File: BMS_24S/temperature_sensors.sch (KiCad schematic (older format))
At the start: 27 parts, among them J1501 TEMP_IDC_26_CONN

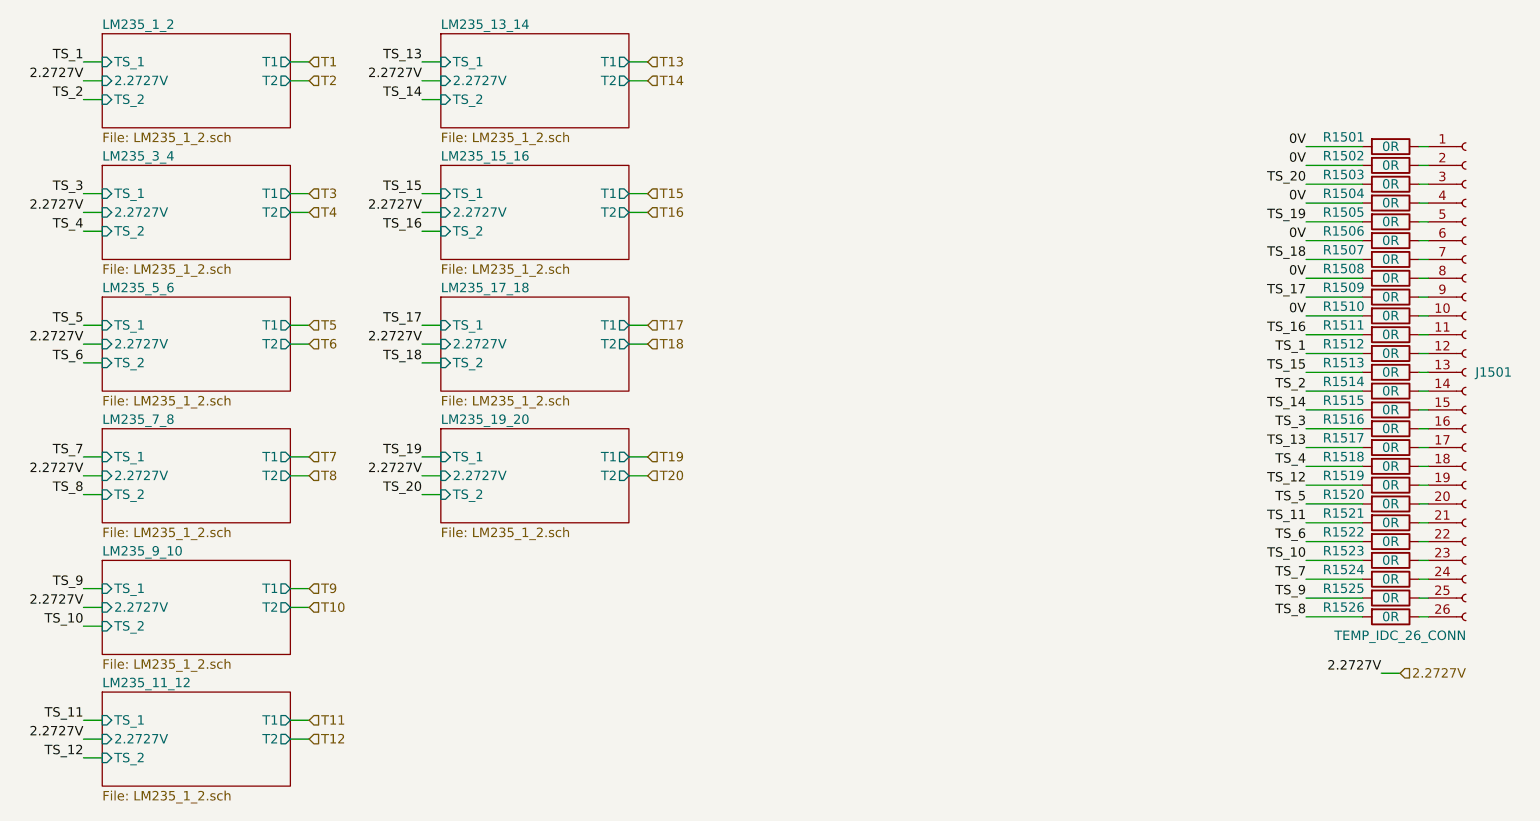
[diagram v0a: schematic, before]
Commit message: update balancing circuit
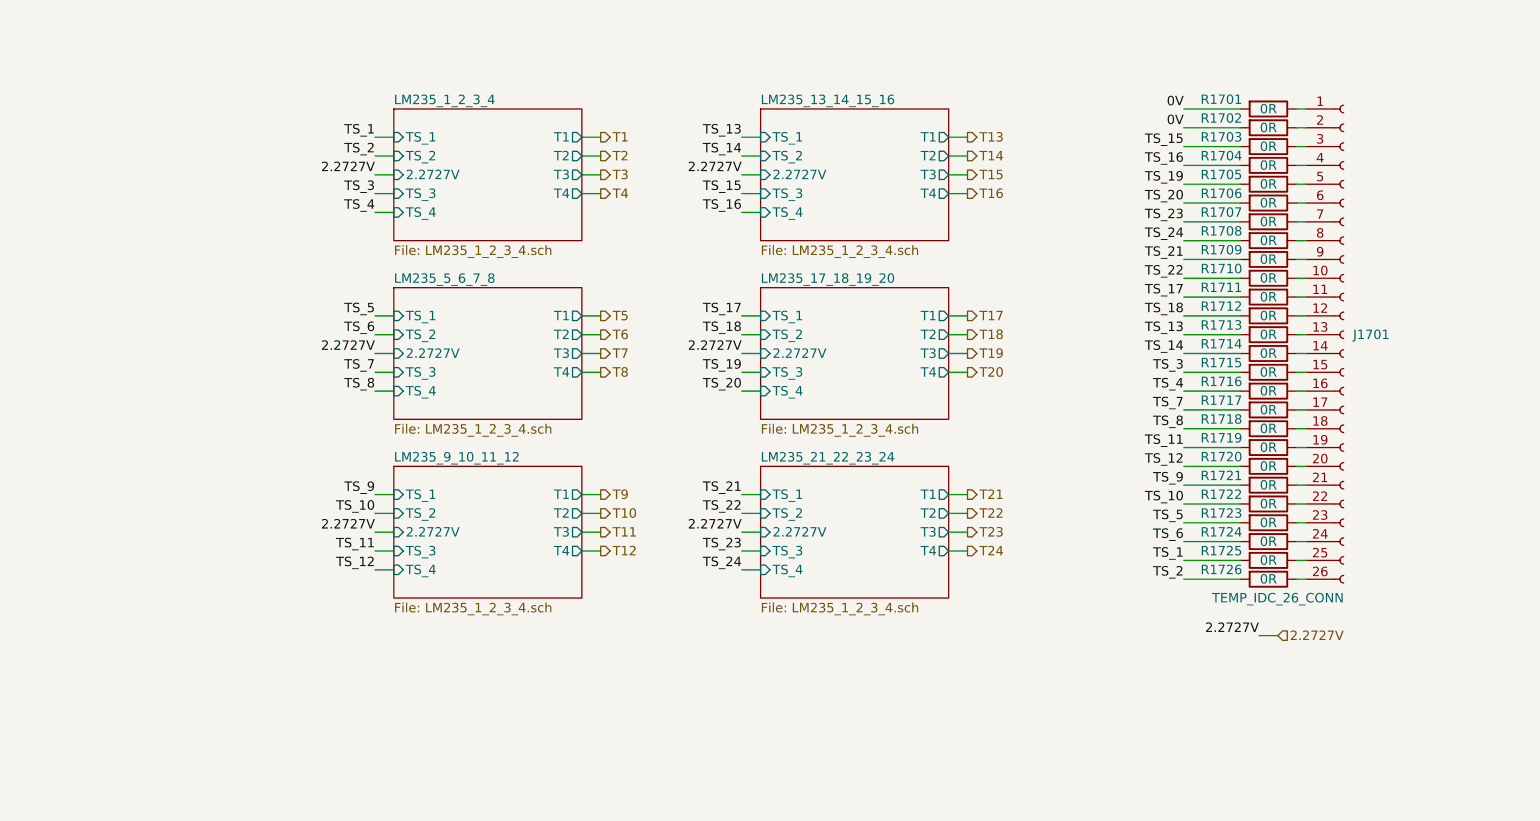
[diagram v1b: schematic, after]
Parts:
- renumbered J1501 to J1701, R1501 to R1701, R1502 to R1702, R1503 to R1703, R1504 to R1704, R1505 to R1705, R1506 to R1706, R1507 to R1707, R1508 to R1708, R1509 to R1709, R1510 to R1710, R1511 to R1711, R1512 to R1712, R1513 to R1713, R1514 to R1714, R1515 to R1715, R1516 to R1716, R1517 to R1717, R1518 to R1718, R1519 to R1719, R1520 to R1720, R1521 to R1721, R1522 to R1722, R1523 to R1723, R1524 to R1724, R1525 to R1725, R1526 to R1726
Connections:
- net 0V: no longer R1704.2, R1706.2, R1708.2, R1710.2
- net TS_1: now also R1725.2; no longer R1712.2
- net TS_10: now also R1722.2; no longer R1723.2
- net TS_11: now also R1719.2; no longer R1721.2
- net TS_12: now also R1720.2; no longer R1719.2
- net TS_13: now also R1713.2; no longer R1717.2
- net TS_14: now also R1714.2; no longer R1715.2
- net TS_15: now also R1703.2; no longer R1713.2
- net TS_16: now also R1704.2; no longer R1711.2
- net TS_17: now also R1711.2; no longer R1709.2
- net TS_18: now also R1712.2; no longer R1707.2
- net TS_2: now also R1726.2; no longer R1714.2
- net TS_20: now also R1706.2; no longer R1703.2
- net TS_3: now also R1715.2; no longer R1716.2
- net TS_4: now also R1716.2; no longer R1718.2
- net TS_5: now also R1723.2; no longer R1720.2
- net TS_6: now also R1724.2; no longer R1722.2
- net TS_7: now also R1717.2; no longer R1724.2
- net TS_8: now also R1718.2; no longer R1726.2
- net TS_9: now also R1721.2; no longer R1725.2
- new net TS_21: R1709.2
- new net TS_22: R1710.2
- new net TS_23: R1707.2
- new net TS_24: R1708.2
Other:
- moved on the sheet: J1701, R1701, R1702, R1703, R1704, R1705, R1706, R1707, R1708, R1709, R1710, R1711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

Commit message: get BSPD
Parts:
- R1701, R1702, R1703, R1704, R1705, R1706, R1707, R1708, R1709, R1710, R1711, R1712, R1713, R1714, R1715, R1716, R1717, R1718, R1719, R1720, R1721, R1722, R1723, R1724, R1725, R1726: LCSC (none) -> C17477
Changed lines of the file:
@@
 F 2 "Resistor_SMD:R_0805_2012Metric" V 7080 1100 50  0001 C CNN
 F 3 "~" H 7150 1100 50  0001 C CNN
+F 4 "C17477" H 7150 1100 50  0001 C CNN "LCSC"
 	1    7150 1100
 	0    1    1    0
@@
 F 2 "Resistor_SMD:R_0805_2012Metric" V 7080 1200 50  0001 C CNN
 F 3 "~" H 7150 1200 50  0001 C CNN
+F 4 "C17477" H 7150 1200 50  0001 C CNN "LCSC"
 	1    7150 1200
 	0    1    1    0
@@
 F 2 "Resistor_SMD:R_0805_2012Metric" V 7080 1300 50  0001 C CNN
 F 3 "~" H 7150 1300 50  0001 C CNN
+F 4 "C17477" H 7150 1300 50  0001 C CNN "LCSC"
 	1    7150 1300
 	0    1    1    0
@@
 F 2 "Resistor_SMD:R_0805_2012Metric" V 7080 1400 50  0001 C CNN
 F 3 "~" H 7150 1400 50  0001 C CNN
+F 4 "C17477" H 7150 1400 50  0001 C CNN "LCSC"
 	1    7150 1400
 	0    1    1    0
@@
 F 2 "Resistor_SMD:R_0805_2012Metric" V 7080 1500 50  0001 C CNN
 F 3 "~" H 7150 1500 50  0001 C CNN
+F 4 "C17477" H 7150 1500 50  0001 C CNN "LCSC"
 	1    7150 1500
 	0    1    1    0
@@
 F 2 "Resistor_SMD:R_0805_2012Metric" V 7080 1600 50  0001 C CNN
 F 3 "~" H 7150 1600 50  0001 C CNN
+F 4 "C17477" H 7150 1600 50  0001 C CNN "LCSC"
 	1    7150 1600
 	0    1    1    0
@@
 F 2 "Resistor_SMD:R_0805_2012Metric" V 7080 1700 50  0001 C CNN
 F 3 "~" H 7150 1700 50  0001 C CNN
+F 4 "C17477" H 7150 1700 50  0001 C CNN "LCSC"
 	1    7150 1700
 	0    1    1    0
@@
 F 2 "Resistor_SMD:R_0805_2012Metric" V 7080 1800 50  0001 C CNN
 F 3 "~" H 7150 1800 50  0001 C CNN
+F 4 "C17477" H 7150 1800 50  0001 C CNN "LCSC"
 	1    7150 1800
 	0    1    1    0
@@
 F 2 "Resistor_SMD:R_0805_2012Metric" V 7080 1900 50  0001 C CNN
 F 3 "~" H 7150 1900 50  0001 C CNN
+F 4 "C17477" H 7150 1900 50  0001 C CNN "LCSC"
 	1    7150 1900
 	0    1    1    0
@@
 F 2 "Resistor_SMD:R_0805_2012Metric" V 7080 2000 50  0001 C CNN
 F 3 "~" H 7150 2000 50  0001 C CNN
+F 4 "C17477" H 7150 2000 50  0001 C CNN "LCSC"
 	1    7150 2000
 	0    1    1    0
@@
 F 2 "Resistor_SMD:R_0805_2012Metric" V 7080 2100 50  0001 C CNN
 F 3 "~" H 7150 2100 50  0001 C CNN
+F 4 "C17477" H 7150 2100 50  0001 C CNN "LCSC"
 	1    7150 2100
 	0    1    1    0
@@
 F 2 "Resistor_SMD:R_0805_2012Metric" V 7080 2400 50  0001 C CNN
 F 3 "~" H 7150 2400 50  0001 C CNN
+F 4 "C17477" H 7150 2400 50  0001 C CNN "LCSC"
 	1    7150 2400
 	0    1    1    0
@@
 F 2 "Resistor_SMD:R_0805_2012Metric" V 7080 2200 50  0001 C CNN
 F 3 "~" H 7150 2200 50  0001 C CNN
+F 4 "C17477" H 7150 2200 50  0001 C CNN "LCSC"
 	1    7150 2200
 	0    1    1    0
@@
 F 2 "Resistor_SMD:R_0805_2012Metric" V 7080 2300 50  0001 C CNN
 F 3 "~" H 7150 2300 50  0001 C CNN
+F 4 "C17477" H 7150 2300 50  0001 C CNN "LCSC"
 	1    7150 2300
 	0    1    1    0
@@
 F 2 "Resistor_SMD:R_0805_2012Metric" V 7080 2500 50  0001 C CNN
 F 3 "~" H 7150 2500 50  0001 C CNN
+F 4 "C17477" H 7150 2500 50  0001 C CNN "LCSC"
 	1    7150 2500
 	0    1    1    0
@@
 F 2 "Resistor_SMD:R_0805_2012Metric" V 7080 2600 50  0001 C CNN
 F 3 "~" H 7150 2600 50  0001 C CNN
+F 4 "C17477" H 7150 2600 50  0001 C CNN "LCSC"
 	1    7150 2600
 	0    1    1    0
@@
 F 2 "Resistor_SMD:R_0805_2012Metric" V 7080 2700 50  0001 C CNN
 F 3 "~" H 7150 2700 50  0001 C CNN
+F 4 "C17477" H 7150 2700 50  0001 C CNN "LCSC"
 	1    7150 2700
 	0    1    1    0
@@
 F 2 "Resistor_SMD:R_0805_2012Metric" V 7080 2800 50  0001 C CNN
 F 3 "~" H 7150 2800 50  0001 C CNN
+F 4 "C17477" H 7150 2800 50  0001 C CNN "LCSC"
 	1    7150 2800
 	0    1    1    0
@@
 F 2 "Resistor_SMD:R_0805_2012Metric" V 7080 2900 50  0001 C CNN
 F 3 "~" H 7150 2900 50  0001 C CNN
+F 4 "C17477" H 7150 2900 50  0001 C CNN "LCSC"
 	1    7150 2900
 	0    1    1    0
@@
 F 2 "Resistor_SMD:R_0805_2012Metric" V 7080 3000 50  0001 C CNN
 F 3 "~" H 7150 3000 50  0001 C CNN
+F 4 "C17477" H 7150 3000 50  0001 C CNN "LCSC"
 	1    7150 3000
 	0    1    1    0
@@
 F 2 "Resistor_SMD:R_0805_2012Metric" V 7080 3100 50  0001 C CNN
 F 3 "~" H 7150 3100 50  0001 C CNN
+F 4 "C17477" H 7150 3100 50  0001 C CNN "LCSC"
 	1    7150 3100
 	0    1    1    0
@@
 F 2 "Resistor_SMD:R_0805_2012Metric" V 7080 3200 50  0001 C CNN
 F 3 "~" H 7150 3200 50  0001 C CNN
+F 4 "C17477" H 7150 3200 50  0001 C CNN "LCSC"
 	1    7150 3200
 	0    1    1    0
@@
 F 2 "Resistor_SMD:R_0805_2012Metric" V 7080 3300 50  0001 C CNN
 F 3 "~" H 7150 3300 50  0001 C CNN
+F 4 "C17477" H 7150 3300 50  0001 C CNN "LCSC"
 	1    7150 3300
 	0    1    1    0
@@
 F 2 "Resistor_SMD:R_0805_2012Metric" V 7080 3400 50  0001 C CNN
 F 3 "~" H 7150 3400 50  0001 C CNN
+F 4 "C17477" H 7150 3400 50  0001 C CNN "LCSC"
 	1    7150 3400
 	0    1    1    0
@@
 F 2 "Resistor_SMD:R_0805_2012Metric" V 7080 3500 50  0001 C CNN
 F 3 "~" H 7150 3500 50  0001 C CNN
+F 4 "C17477" H 7150 3500 50  0001 C CNN "LCSC"
 	1    7150 3500
 	0    1    1    0
@@
 F 2 "Resistor_SMD:R_0805_2012Metric" V 7080 1000 50  0001 C CNN
 F 3 "~" H 7150 1000 50  0001 C CNN
+F 4 "C17477" H 7150 1000 50  0001 C CNN "LCSC"
 	1    7150 1000
 	0    1    1    0
